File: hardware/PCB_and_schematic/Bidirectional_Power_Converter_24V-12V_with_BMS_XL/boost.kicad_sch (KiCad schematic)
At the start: 6 parts, among them U2 LM358

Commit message: buck boost progress
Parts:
- added C1, C2: 100n, Resistor_SMD:R_0805_2012Metric_Pad1.20x1.40mm_HandSolder, symbol Device:C
- added C5: 1000u/35V, Capacitor_THT:CP_Radial_D10.0mm_P3.50mm, symbol Device:C_Polarized
- added D5: D_Schottky_Dua, My-Footprints:TO-220-3_Vertical-little-bigger pads, symbol Device:D_Schottky_Dual_CommonAnode_AKK_Parallel
- added L1: 60uH (100kHz), Inductor_THT:L_Toroid_Vertical_L28.6mm_W14.3mm_P11.43mm_Bourns_5700, symbol Device:L
- added R17, R19: 1k, Resistor_SMD:R_0805_2012Metric, symbol Device:R
- added U3: LM358, Package_DIP:CERDIP-8_W7.62mm_SideBrazed_LongPads, symbol Amplifier_Operational:LM358
- D2: footprint (none) -> Diode_SMD:D_MiniMELF
- D3: renamed from D16; footprint (none) -> Diode_SMD:D_MiniMELF
- U1: renamed from U2; footprint (none) -> Package_DIP:CERDIP-8_W7.62mm_SideBrazed_LongPads
- renumbered R24 to R13, R23 to R14, R20 to R18
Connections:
- net BOOST_CURRENT_FB: now also C2.1, U3.3 (+)
- net GND: now also C1.2, C2.2, R17.2
- new net: R17.1, R19.2, U3.2 (-)
- new net: D5.1 (A), L1.2
- new net +5V: C1.1
- new net PV_VOLTAGE_POSITIVE: C5.1, D5.2 (K), D5.3 (K)
- new net VREF_2.5V: R19.1
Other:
- moved on the sheet: D3, R13, R14, R18, U1A

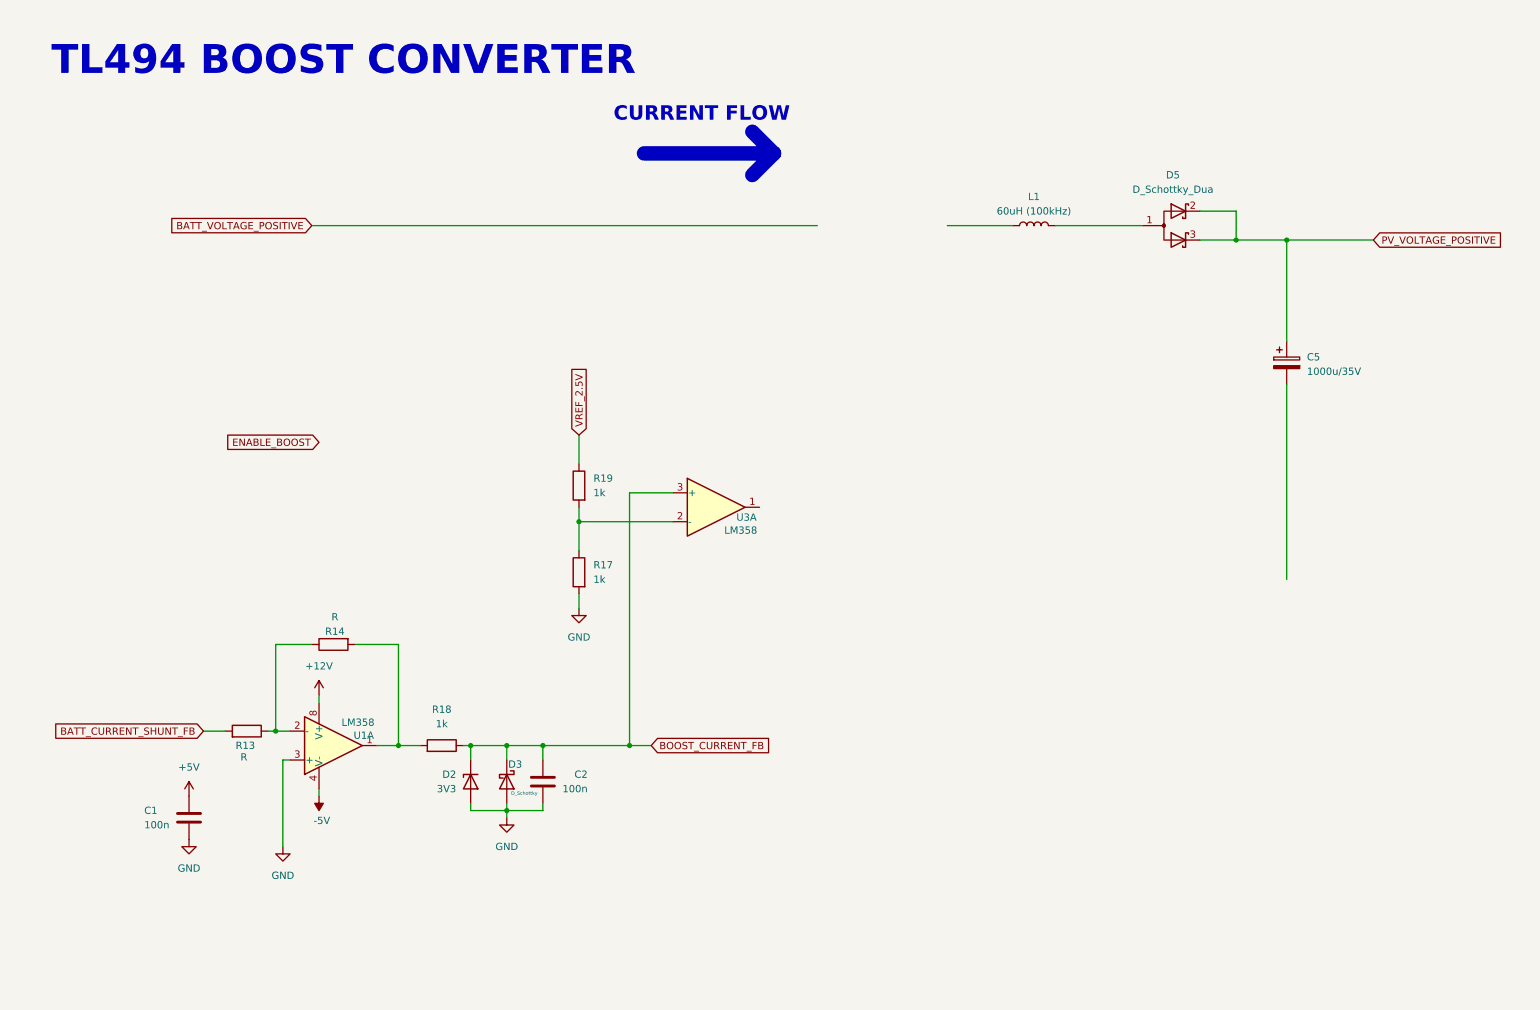
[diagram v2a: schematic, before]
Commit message: boost converter xl6019 schematic
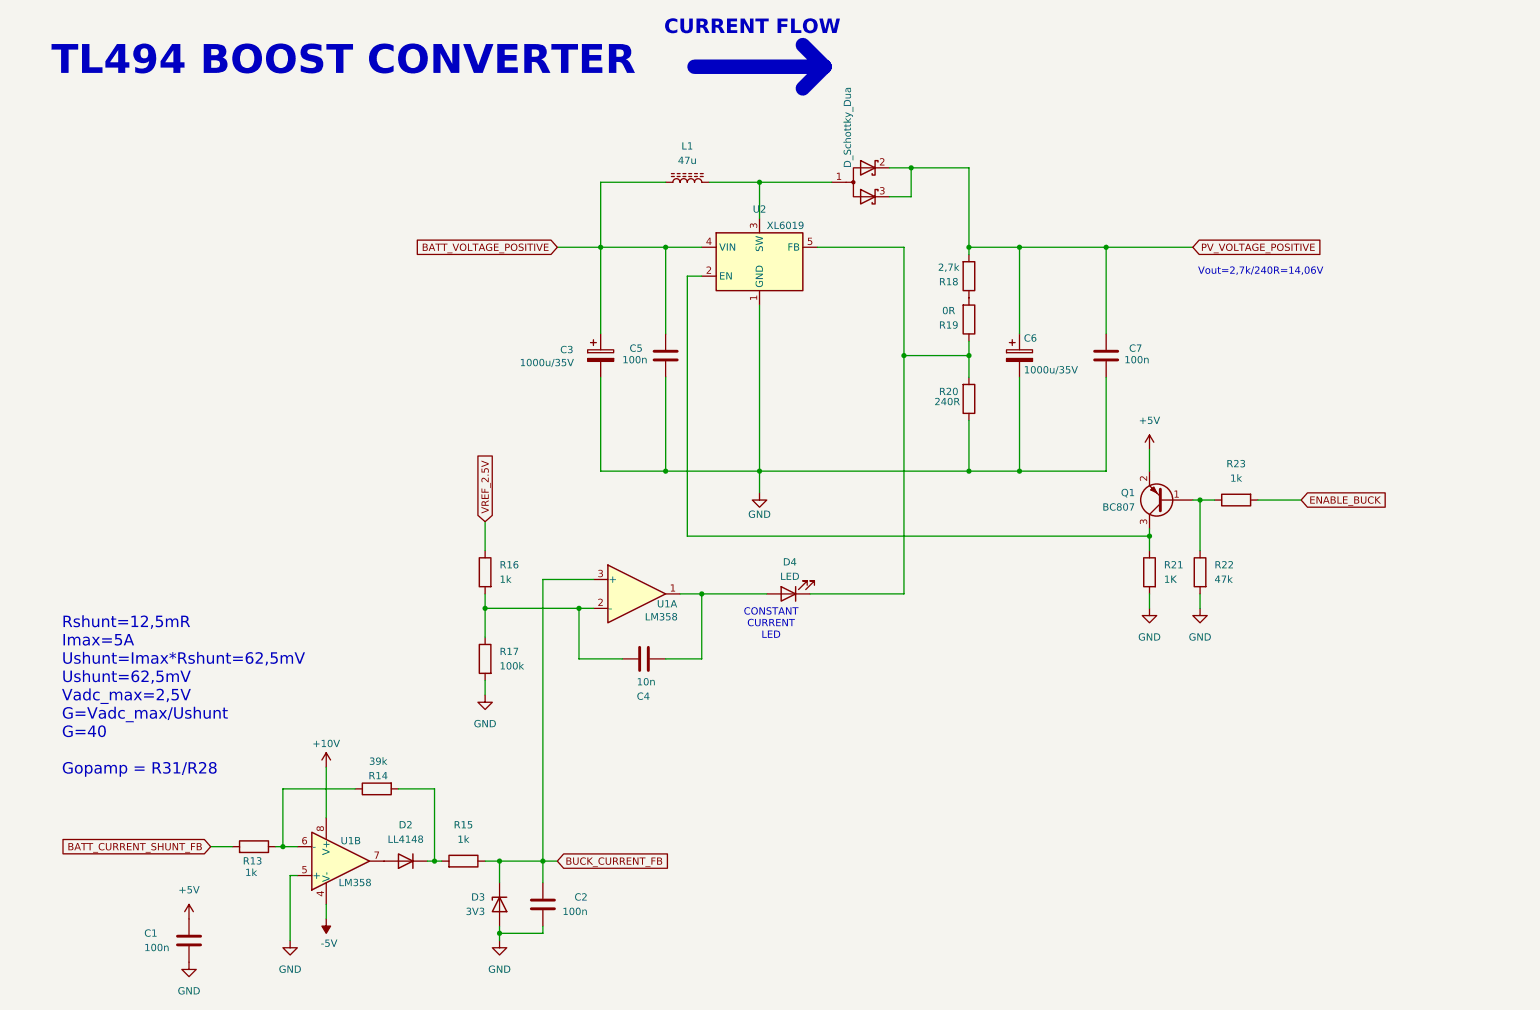
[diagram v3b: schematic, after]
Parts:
- removed C5: 1000u/35V, Capacitor_THT:CP_Radial_D10.0mm_P3.50mm, symbol Device:C_Polarized
- removed D2: 3V3, Diode_SMD:D_MiniMELF, symbol Device:D_Zener
- removed D3: D_Schottky, Diode_SMD:D_MiniMELF, symbol Device:D_Schottky
- removed L1: 60uH (100kHz), Inductor_THT:L_Toroid_Vertical_L28.6mm_W14.3mm_P11.43mm_Bourns_5700, symbol Device:L
- removed U3: LM358, Package_DIP:CERDIP-8_W7.62mm_SideBrazed_LongPads, symbol Amplifier_Operational:LM358
- added C3, C6: 1000u/35V, Capacitor_THT:CP_Radial_D10.0mm_P3.50mm, symbol Device:C_Polarized
- added C4: 10n, Resistor_SMD:R_0805_2012Metric_Pad1.20x1.40mm_HandSolder, symbol Device:C
- added C5, C7: 100n, Capacitor_SMD:C_0805_2012Metric_Pad1.18x1.45mm_HandSolder, symbol Device:C
- added D2: LL4148, Diode_SMD:D_MiniMELF, symbol Diode:LL4148
- added D3: 3V3, Diode_SMD:D_MiniMELF, symbol Device:D_Zener
- added D4: LED, LED_THT:LED_D3.0mm, symbol Device:LED
- added L1: 47u, Inductor_THT:L_Toroid_Vertical_L28.6mm_W14.3mm_P11.43mm_Bourns_5700, symbol Device:L_Ferrite
- added Q1: BC807, Package_TO_SOT_SMD:SOT-23, symbol Transistor_BJT:BC807
- added R15, R16, R23: 1k, Resistor_SMD:R_0805_2012Metric_Pad1.20x1.40mm_HandSolder, symbol Device:R
- added R20: 240R, Resistor_SMD:R_0805_2012Metric_Pad1.20x1.40mm_HandSolder, symbol Device:R
- added R21: 1K, Resistor_SMD:R_0805_2012Metric_Pad1.20x1.40mm_HandSolder, symbol Device:R
- added R22: 47k, Resistor_SMD:R_0805_2012Metric_Pad1.20x1.40mm_HandSolder, symbol Device:R
- added unit 2 of U1
- added U2: XL6019, Package_TO_SOT_SMD:TO-263-5_TabPin3, symbol My-Lib:XL6019
- R13: value R -> 1k; footprint Resistor_SMD:R_0805_2012Metric -> Resistor_SMD:R_0805_2012Metric_Pad1.20x1.40mm_HandSolder
- R14: value R -> 39k; footprint Resistor_SMD:R_0805_2012Metric -> Resistor_SMD:R_0805_2012Metric_Pad1.20x1.40mm_HandSolder
- R17: value 1k -> 100k; footprint Resistor_SMD:R_0805_2012Metric -> Resistor_SMD:R_0805_2012Metric_Pad1.20x1.40mm_HandSolder
- R18: value 1k -> 2,7k; footprint Resistor_SMD:R_0805_2012Metric -> Resistor_SMD:R_0805_2012Metric_Pad1.20x1.40mm_HandSolder
- R19: value 1k -> 0R; footprint Resistor_SMD:R_0805_2012Metric -> Resistor_SMD:R_0805_2012Metric_Pad1.20x1.40mm_HandSolder
- U1: footprint Package_DIP:CERDIP-8_W7.62mm_SideBrazed_LongPads -> Package_SO:SO-8_3.9x4.9mm_P1.27mm
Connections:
- net +5V: now also Q1.2 (E)
- net BATT_VOLTAGE_POSITIVE: now also C3.1, C5.1, L1.1, U2.4 (VIN)
- net GND: now also C3.2, C5.2, C6.2, C7.2, D3.2 (A), R20.1, R21.2, R22.2, U1.5 (+), U2.1 (GND); no longer U1.3 (+)
- net PV_VOLTAGE_POSITIVE: now also R18.2, C6.1, C7.1
- net VREF_2.5V: now also R16.1; no longer R19.1
- net at R17.1: now also U1.2 (-), C4.2, R16.2; no longer R19.2
- net at D5.1 (A): now also L1.2, U2.3 (SW)
- net at R13.1, R14.1: now also U1.6 (-); no longer U1.2 (-)
- net +12V renamed +10V
- net BOOST_CURRENT_FB: no longer names the net of R18.1
- net BOOST_CURRENT_FB: now also R19.2; no longer C2.1
- new net: D2.1 (K), R14.2, R15.2
- new net: Q1.3 (C), R21.1, U2.2 (EN)
- new net: D4.1 (K), R19.1, R20.2, U2.5 (FB)
- new net: C4.1, D4.2 (A), U1.1
- new net: Q1.1 (B), R22.1, R23.1
- new net: D2.2 (A), U1.7
- new net BUCK_CURRENT_FB: C2.1, D3.1 (K), R15.1, U1.3 (+)
- new net ENABLE_BUCK: R23.2
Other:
- note added: "CONSTANT CURRENT LED"
- note added: "Rshunt=12,5mR Imax=5A Ushunt=Imax*Rshunt=62,5mV Ushunt=62,5mV Vadc_max=2,5V G=Vadc_max/Ushunt G=40 Gopamp = R31/R28"
- note added: "Vout=2,7k/240R=14,06V"

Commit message: XL smps pcb routing
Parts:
- removed D5: D_Schottky_Dua, My-Footprints:TO-220-3_Vertical-little-bigger pads, symbol Device:D_Schottky_Dual_CommonAnode_AKK_Parallel
- added C34: 1000u/35V, Capacitor_THT:CP_Radial_D10.0mm_P3.50mm, symbol Device:C_Polarized
- added C35: 100n, Resistor_SMD:R_0805_2012Metric_Pad1.20x1.40mm_HandSolder, symbol Device:C
- added D5: D_Schottky_Dual, My-Footprints:TO-220-3_Vertical-little-bigger pads, symbol Device:D_Schottky_Dual_CommonAnode_KAK_Parallel
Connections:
- net +10V: now also C1.1
- net +5V: no longer C1.1
- net -5V: now also C35.1
- net GND: now also C34.2, C35.2
- net PV_VOLTAGE_POSITIVE: now also C34.1, D5.1 (K), D5.3 (K)
- net at L1.2, U2.3 (SW): now also D5.2 (A)
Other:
- moved on the sheet: C7, Q1, R21, R22, R23
